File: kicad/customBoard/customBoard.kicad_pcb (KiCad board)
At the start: 2 copper layers, 158.3 x 110 mm, 80 parts, among them J1 USB4125-GF-A_REVA2, J10 FFC3B07-20-T, J2 PREC002SAAN-RC, J3 SS-53000-001, J4 FFC3B07-20-T, J5 Micro_SD_Card_Det, J6 ARJM11D7-502-AB-EW2, J7 SS-52100-001, J8 SS-52100-001, J9 SS-52100-001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

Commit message: Generate Gerbers
Off to JLCPCB!
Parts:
- renumbered Module1 to CM4
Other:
- board text added: "Dylan Lathrum Thesis Project v1"
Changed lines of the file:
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@@
     (solder_mask_min_width 0.12)
     (pcbplotparams
-      (layerselection 0x00010fc_ffffffff)
+      (layerselection 0x00010f0_ffffffff)
       (disableapertmacros false)
       (usegerberextensions false)
@@
       (psa4output false)
       (plotreference true)
-      (plotvalue true)
+      (plotvalue false)
       (plotinvisibletext false)
       (sketchpadsonfab false)
@@
     (fp_line (start -1.6 0.8) (end 1.6 0.8) (layer "F.Fab") (width 0.1))
     (fp_line (start 1.6 -0.8) (end -1.2 -0.8) (layer "F.Fab") (width 0.1))
-    (pad "1" smd roundrect locked (at -1.4875 0 90) (size 1.425 1.75) (layers "F.Cu" "F.Paste" "F.Mask") (roundrect_rratio 0.175439)
+    (pad "1" smd roundrect locked (at -1.4875 0 90) (size 1.425 1.75) (layers "F.Cu" "F.Paste" "F.Mask") (roundrect_rratio 0.1754392982)
       (net 11 "Net-(D2-Pad1)") (pinfunction "K") (pintype "passive"))
-    (pad "2" smd roundrect locked (at 1.4875 0 90) (size 1.425 1.75) (layers "F.Cu" "F.Paste" "F.Mask") (roundrect_rratio 0.175439)
+    (pad "2" smd roundrect locked (at 1.4875 0 90) (size 1.425 1.75) (layers "F.Cu" "F.Paste" "F.Mask") (roundrect_rratio 0.1754392982)
       (net 1 "GND") (pinfunction "A") (pintype "passive"))
     (model "${KICAD6_3DMODEL_DIR}/LED_SMD.3dshapes/LED_1206_3216Metric.wrl"
@@
     (fp_line (start 1.6 0.8) (end 1.6 -0.8) (layer "F.Fab") (width 0.1))
     (fp_line (start -1.6 -0.4) (end -1.6 0.8) (layer "F.Fab") (width 0.1))
-    (pad "1" smd roundrect locked (at -1.4875 0) (size 1.425 1.75) (layers "F.Cu" "F.Paste" "F.Mask") (roundrect_rratio 0.175439)
+    (pad "1" smd roundrect locked (at -1.4875 0) (size 1.425 1.75) (layers "F.Cu" "F.Paste" "F.Mask") (roundrect_rratio 0.1754392982)
       (net 16 "Net-(D6-Pad1)") (pinfunction "K") (pintype "passive"))
-    (pad "2" smd roundrect locked (at 1.4875 0) (size 1.425 1.75) (layers "F.Cu" "F.Paste" "F.Mask") (roundrect_rratio 0.175439)
+    (pad "2" smd roundrect locked (at 1.4875 0) (size 1.425 1.75) (layers "F.Cu" "F.Paste" "F.Mask") (roundrect_rratio 0.1754392982)
       (net 14 "+3V3") (pinfunction "A") (pintype "passive"))
     (model "${KICAD6_3DMODEL_DIR}/LED_SMD.3dshapes/LED_1206_3216Metric.wrl"
@@
     (fp_line (start 1.6 -0.8) (end -1.2 -0.8) (layer "F.Fab") (width 0.1))
     (fp_line (start 1.6 0.8) (end 1.6 -0.8) (layer "F.Fab") (width 0.1))
-    (pad "1" smd roundrect locked (at -1.4875 0 90) (size 1.425 1.75) (layers "F.Cu" "F.Paste" "F.Mask") (roundrect_rratio 0.175439)
+    (pad "1" smd roundrect locked (at -1.4875 0 90) (size 1.425 1.75) (layers "F.Cu" "F.Paste" "F.Mask") (roundrect_rratio 0.1754392982)
       (net 12 "Net-(D3-Pad1)") (pinfunction "K") (pintype "passive"))
-    (pad "2" smd roundrect locked (at 1.4875 0 90) (size 1.425 1.75) (layers "F.Cu" "F.Paste" "F.Mask") (roundrect_rratio 0.175439)
+    (pad "2" smd roundrect locked (at 1.4875 0 90) (size 1.425 1.75) (layers "F.Cu" "F.Paste" "F.Mask") (roundrect_rratio 0.1754392982)
       (net 4 "VBUS") (pinfunction "A") (pintype "passive"))
     (model "${KICAD6_3DMODEL_DIR}/LED_SMD.3dshapes/LED_1206_3216Metric.wrl"
@@
     (property "Sheetname" "CM4")
     (attr smd)
-    (fp_text reference "Module1" (at 16.51 -0.254 180) (layer "F.SilkS")
+    (fp_text reference "CM4" (at 16.51 0.006 180) (layer "F.SilkS")
       (effects (font (size 1 1) (thickness 0.15)))
     )
@@
     (fp_line (start 1.6 -0.8) (end -1.2 -0.8) (layer "F.Fab") (width 0.1))
     (fp_line (start -1.6 0.8) (end 1.6 0.8) (layer "F.Fab") (width 0.1))
-    (pad "1" smd roundrect locked (at -1.4875 0 270) (size 1.425 1.75) (layers "F.Cu" "F.Paste" "F.Mask") (roundrect_rratio 0.175439)
+    (pad "1" smd roundrect locked (at -1.4875 0 270) (size 1.425 1.75) (layers "F.Cu" "F.Paste" "F.Mask") (roundrect_rratio 0.1754392982)
       (net 13 "Net-(D4-Pad1)") (pinfunction "K") (pintype "passive"))
-    (pad "2" smd roundrect locked (at 1.4875 0 270) (size 1.425 1.75) (layers "F.Cu" "F.Paste" "F.Mask") (roundrect_rratio 0.175439)
+    (pad "2" smd roundrect locked (at 1.4875 0 270) (size 1.425 1.75) (layers "F.Cu" "F.Paste" "F.Mask") (roundrect_rratio 0.1754392982)
       (net 4 "VBUS") (pinfunction "A") (pintype "passive"))
     (model "${KICAD6_3DMODEL_DIR}/LED_SMD.3dshapes/LED_1206_3216Metric.wrl"
@@
     (fp_line (start -1.6 0.8) (end 1.6 0.8) (layer "F.Fab") (width 0.1))
     (fp_line (start 1.6 0.8) (end 1.6 -0.8) (layer "F.Fab") (width 0.1))
-    (pad "1" smd roundrect locked (at -1.4875 0 270) (size 1.425 1.75) (layers "F.Cu" "F.Paste" "F.Mask") (roundrect_rratio 0.175439)
+    (pad "1" smd roundrect locked (at -1.4875 0 270) (size 1.425 1.75) (layers "F.Cu" "F.Paste" "F.Mask") (roundrect_rratio 0.1754392982)
       (net 1 "GND") (pinfunction "K") (pintype "passive"))
-    (pad "2" smd roundrect locked (at 1.4875 0 270) (size 1.425 1.75) (layers "F.Cu" "F.Paste" "F.Mask") (roundrect_rratio 0.175439)
+    (pad "2" smd roundrect locked (at 1.4875 0 270) (size 1.425 1.75) (layers "F.Cu" "F.Paste" "F.Mask") (roundrect_rratio 0.1754392982)
       (net 10 "Net-(D1-Pad2)") (pinfunction "A") (pintype "passive"))
     (model "${KICAD6_3DMODEL_DIR}/LED_SMD.3dshapes/LED_1206_3216Metric.wrl"
@@
     (fp_line (start -1.2 -0.8) (end -1.6 -0.4) (layer "F.Fab") (width 0.1))
     (fp_line (start -1.6 -0.4) (end -1.6 0.8) (layer "F.Fab") (width 0.1))
-    (pad "1" smd roundrect locked (at -1.4875 0 180) (size 1.425 1.75) (layers "F.Cu" "F.Paste" "F.Mask") (roundrect_rratio 0.175439)
+    (pad "1" smd roundrect locked (at -1.4875 0 180) (size 1.425 1.75) (layers "F.Cu" "F.Paste" "F.Mask") (roundrect_rratio 0.1754392982)
       (net 15 "Net-(D5-Pad1)") (pinfunction "K") (pintype "passive"))
-    (pad "2" smd roundrect locked (at 1.4875 0 180) (size 1.425 1.75) (layers "F.Cu" "F.Paste" "F.Mask") (roundrect_rratio 0.175439)
+    (pad "2" smd roundrect locked (at 1.4875 0 180) (size 1.425 1.75) (layers "F.Cu" "F.Paste" "F.Mask") (roundrect_rratio 0.1754392982)
       (net 14 "+3V3") (pinfunction "A") (pintype "passive"))
     (model "${KICAD6_3DMODEL_DIR}/LED_SMD.3dshapes/LED_1206_3216Metric.wrl"
@@
   (gr_line (start 185.7 20.35) (end 185.7 127.35) (layer "Edge.Cuts") (width 0.0381))
   (gr_arc (start 182.7 127.35) (end 182.7 130.35) (angle -90) (layer "Edge.Cuts") (width 0.0381))
+  (gr_text "Dylan Lathrum\nThesis Project\nv1" (at 86.2 57.7) (layer "F.SilkS")
+    (effects (font (size 0.8128 0.8128) (thickness 0.1524)))
+  )
   (segment (start 42.772 34.203) (end 42.282 34.203) (width 0.127) (layer "F.Cu") (net 1))
   (segment (start 161.243999 90.943999) (end 160.5 90.2) (width 0.127) (layer "F.Cu") (net 1))

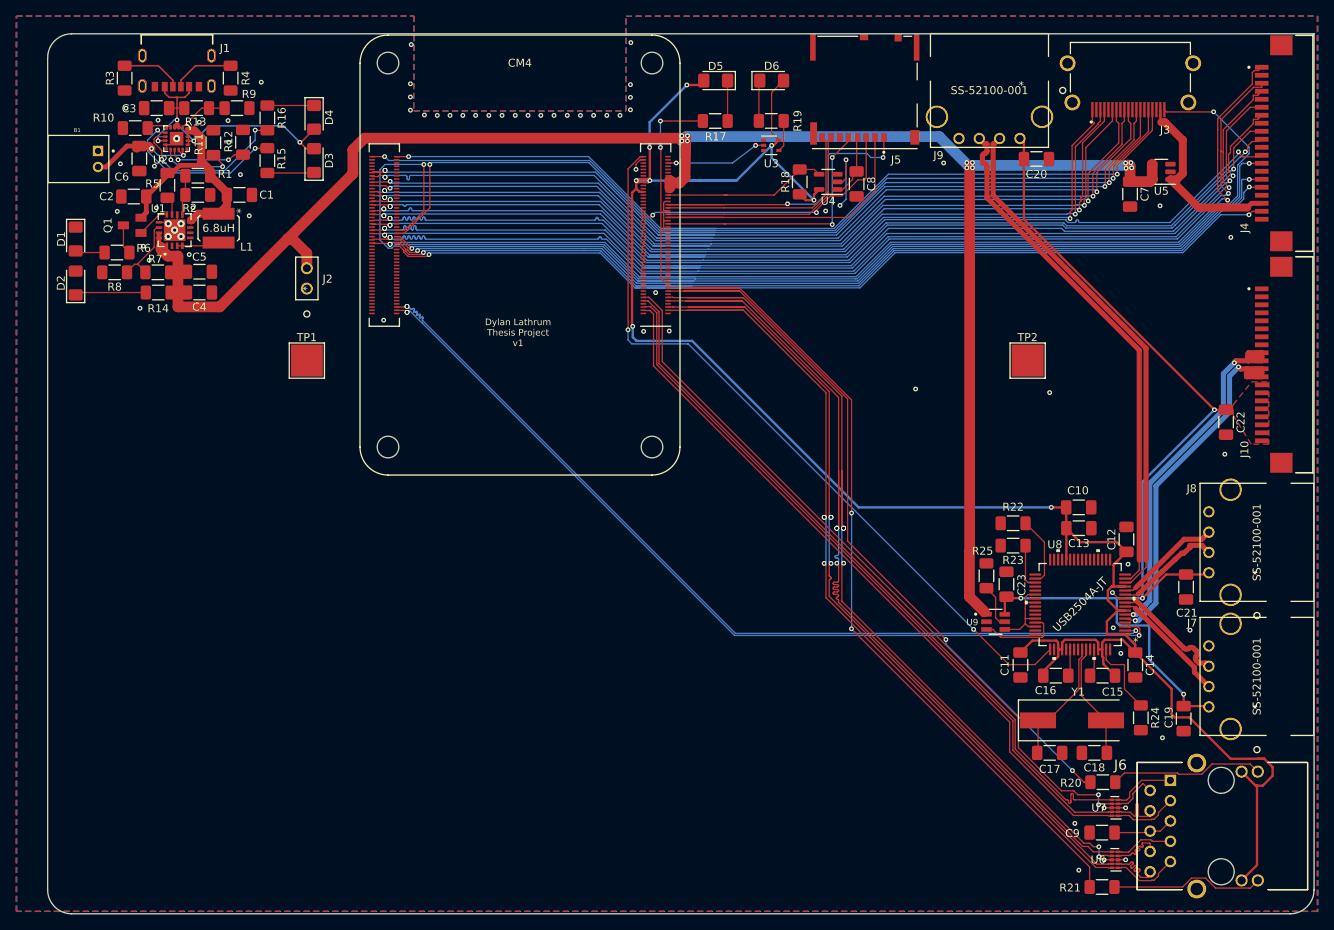
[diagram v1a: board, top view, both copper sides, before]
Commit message: Version 2 of board
Fix U2 to use the footprint "QFN-20-1EP_4x4mm_RevA" instead of "QFN-20-1EP_4x4mm"
Rotate J5 by 180 degrees
Slight aesthetic tweaks
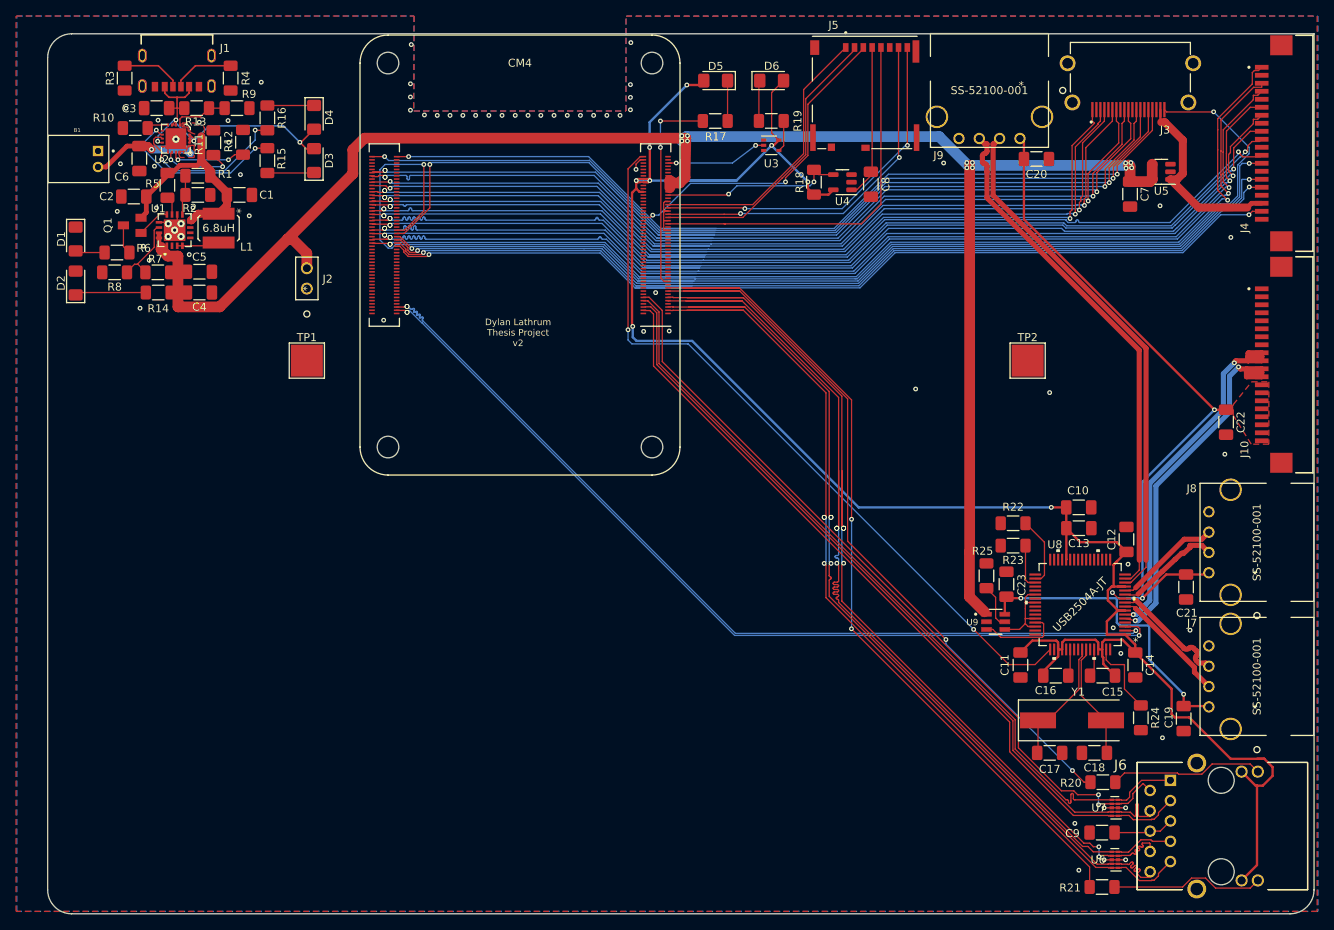
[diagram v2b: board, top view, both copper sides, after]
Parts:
- U2: footprint digikey-footprints:QFN-20-1EP_4x4mm -> digikey-footprints:QFN-20-1EP_4x4mm_RevA
- moved C8 1.78 mm to (130.3, 39.2)
- moved R18 1.78 mm to (123.2, 38.9)
- moved U4 1.78 mm to (126.7, 38.9)
- moved U2 0.09 mm to (43.4, 33.5)
- turned J5 to 0 degrees
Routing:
- net /CM4/SD_DAT1: track 27.7 -> 45.5 mm, vias 0 -> 2
- net /CM4/SD_DAT0: track 28.4 -> 45.6 mm, vias 0 -> 2
- net /CM4/SD_CLK: track 32.4 -> 47.4 mm, vias 2 -> 0
- net Net-(C8-Pad1): track 7.93 -> 19.2 mm
- net GND: track 31.3 -> 21.0 mm, vias 73 -> 70
- net /CM4/SD_DAT2: track 42.0 -> 35.0 mm, vias 2 -> 0
- net /CM4/SD_CMD: track 35.2 -> 40.4 mm
- net /CM4/SD_DAT3: track 41.0 -> 36.4 mm
- net Net-(Module1-Pad75): track 20.8 -> 23.1 mm, vias 0 -> 2
- net Net-(B1-Pad2): track 15.3 -> 13.1 mm
- net VBAT: track 28.9 -> 27.1 mm
- net +3V3: track 262.4 -> 260.7 mm
- added copper zone on F.Cu, net Net-(B1-Pad2)
- added copper zone on F.Cu, net VBAT
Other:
- board text added: "Dylan Lathrum Thesis Project v2"
- board text removed: "Dylan Lathrum Thesis Project v1"
